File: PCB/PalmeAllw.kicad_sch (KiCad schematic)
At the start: 0 parts

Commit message: Sch in progress, eMMC added
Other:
- added sheet GPS (GPS.kicad_sch)
- added sheet LCD (LCD.kicad_sch)
- added sheet LORA (Lora.kicad_sch)
- added sheet RAM (LPDDR3.kicad_sch)
- added sheet STM32 (stm32.kicad_sch)
- added sheet USB (usb.kicad_sch)
- added sheet WiFiBt (WiFiBt.kicad_sch)
- added sheet eMMC (eMMC.kicad_sch)
- added sheet uSD (uSD.kicad_sch)
- sheet CPU ports: added +AVCCPLL, +VCC1V2HSIC, +VCC3V3VID, +VCCIO3V3, +VCCPL1V8, +VCCRTC, +VDD1V8, +VDDCPUS1V1, +VDDCPUX, +VDDSYS1V1, 5VEN, AP_CK32KO, AP_NMI, AP_RESET, BTN_PWRON, PMUBUS, USB0, USB1, VDDFB-CPUX; removed none
- sheet Power ports: added +AVCCPLL, +USBVIN, +USBVOUT, +VCC1V2HSIC, +VCC3V3VID, +VCCIO3V3, +VCCPL1V8, +VCCRTC, +VCC_DRAM, +VDD1V8, +VDDCPUS1V1, +VDDCPUX, +VDDSYS1V1, 5VEN, AP_NMI, AP_RESET, BTN_PWRON, PMUBUS, USB0, VDDFB-CPUX; removed none

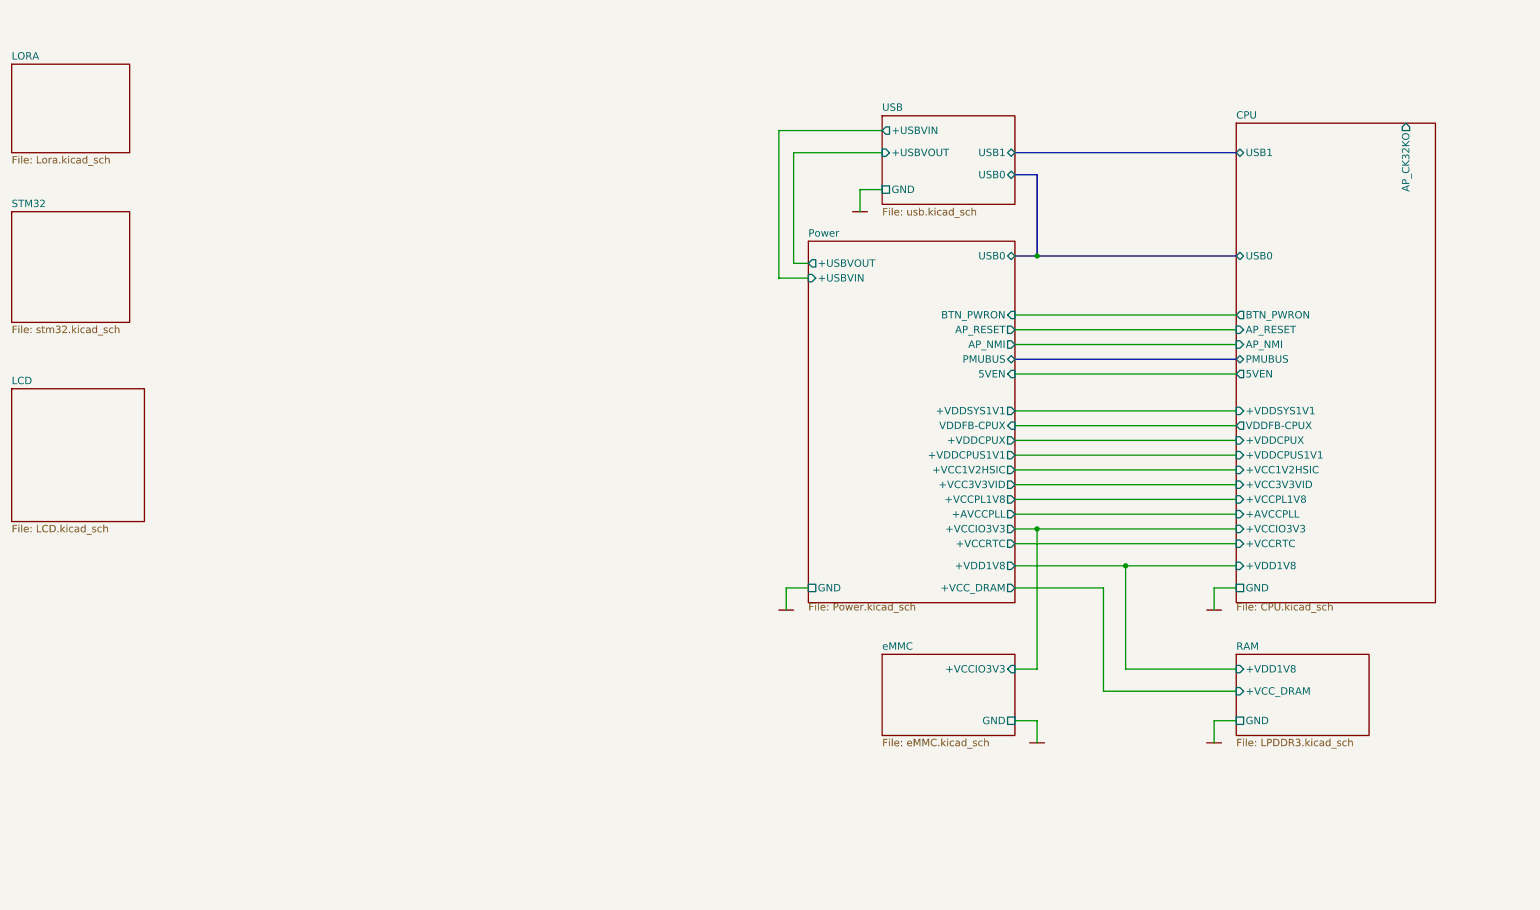
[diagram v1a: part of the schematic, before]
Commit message: + LCD
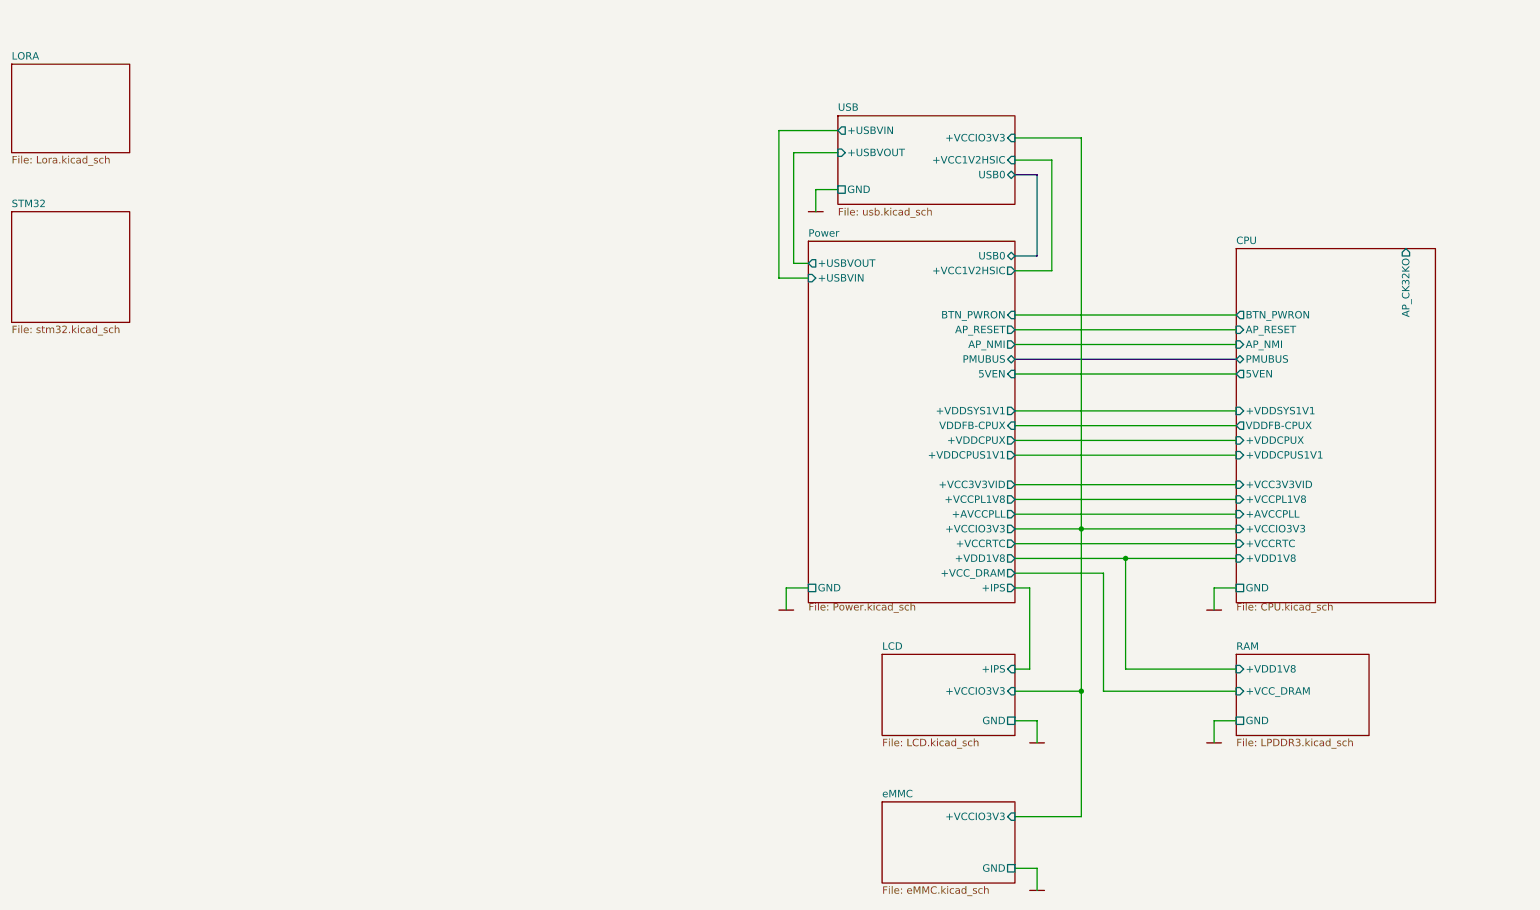
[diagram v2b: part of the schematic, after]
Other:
- sheet CPU ports: added none; removed +VCC1V2HSIC, USB0, USB1
- sheet LCD ports: added +IPS, +VCCIO3V3, GND; removed none
- sheet Power ports: added +IPS; removed none
- sheet USB ports: added +VCC1V2HSIC, +VCCIO3V3; removed USB1

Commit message: Before eMMC removing
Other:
- sheet CPU ports: added TOUCH; removed none
- sheet LCD ports: added TOUCH; removed none
